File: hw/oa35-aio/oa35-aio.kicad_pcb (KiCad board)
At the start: 6 copper layers, 36 x 36 mm, 283 parts, among them J1 TYPE-C-31-M-12, J10 M1A, J11 M1B, J12 M1C, J13 M2A, J14 M2B, J15 M2C, J16 M3A, J17 M3B, J18 M3C, J19 M4A, J2 SM06B-SRSS-TB, J20 M4B, J21 M4C, J3 BAT+, J4 BAT-, P1 +5V, P10 TX6, P11 RX1, P12 TX1, P13 LED, P14 BZ-, P15 BZ+, P16 RSSI, P17 SCL, P18 SDA, P19 +3V3, P2 GND, P20 GND, P21 VBAT, P22 GND, P3 RX2, P4 TX2, P5 +5V, P6 GND, P7 RX4, P8 TX4, P9 RX6, Q1 2N7002, U1 INA186A3IDCKR, U10 USBLC6-2SC6, U2 LMR51430YFDDCR, U20 AT32F421G8U7, U21 NSG2065Q, U3 LMR51430YFDDCR, U30 AT32F421G8U7, U31 NSG2065Q, U4 LP5912-3.3DRVR, U40 AT32F421G8U7, U41 NSG2065Q, U5 TLV76733DRVR, U50 AT32F421G8U7, U51 NSG2065Q, U6 STM32F722RET6, U7 ICM-42688-P, U8 BMP280, U9 W25Q128JVSIQ, Y1 8MHz

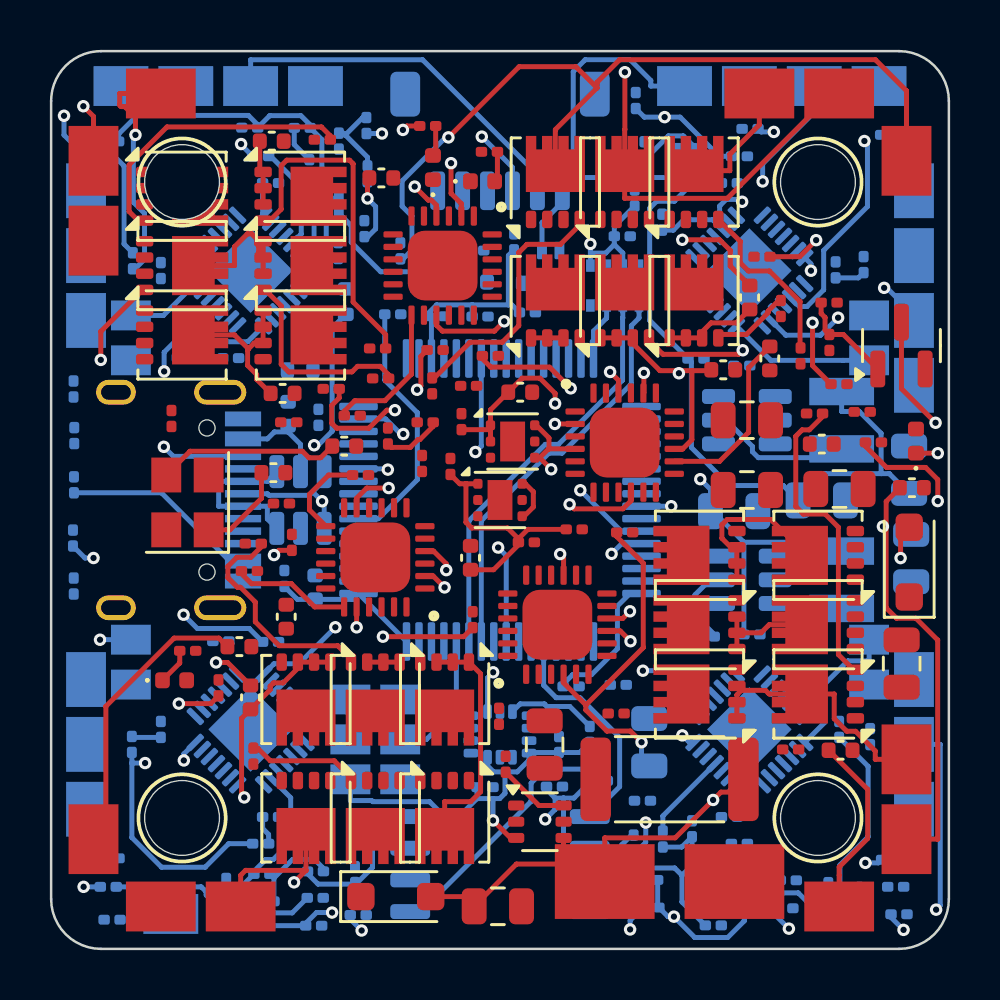
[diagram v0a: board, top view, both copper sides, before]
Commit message: OA35-AIO: regenerate the board at the tighter design rules
Co-Authored-By: Claude Opus 5 <noreply@anthropic.com>
Claude-Session: https://claude.ai/code/session_013J1rgXZWykCJN7jVVS67P2
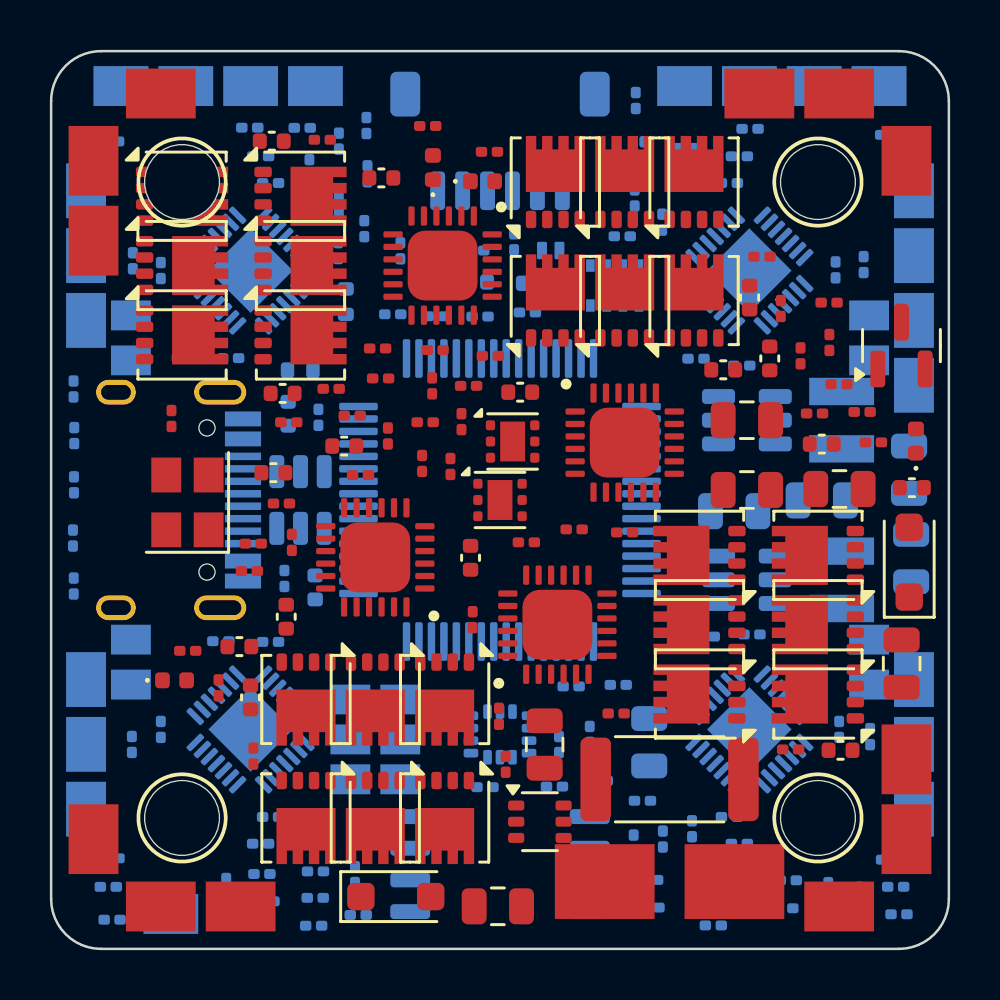
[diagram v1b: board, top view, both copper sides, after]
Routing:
- net +3V3E: track 114.1 -> 0.00 mm, vias 6 -> 0
- net +10V: track 90.3 -> 0.00 mm, vias 8 -> 0
- net +3V3: track 78.3 -> 0.00 mm, vias 4 -> 0
- net PH_B_1: track 49.6 -> 0.00 mm, vias 3 -> 0
- net PH_B_2: track 38.1 -> 0.00 mm, vias 2 -> 0
- net UART1_RX: track 37.3 -> 0.00 mm, vias 3 -> 0
- net PAD_RSSI: track 35.3 -> 0.00 mm, vias 2 -> 0
- net PH_C_2: track 35.3 -> 0.00 mm, vias 1 -> 0
- net PH_B_4: track 34.9 -> 0.00 mm, vias 3 -> 0
- net PAD_BZ-: track 32.3 -> 0.00 mm, vias 2 -> 0
- net VBAT_IN: track 31.7 -> 0.00 mm, vias 2 -> 0
- net ADC_RSSI: track 29.8 -> 0.00 mm, vias 2 -> 0
- net +5V_BUCK: track 28.7 -> 0.00 mm
- net UART4_RX: track 25.9 -> 0.00 mm, vias 2 -> 0
- net FBB_1: track 25.8 -> 0.00 mm, vias 3 -> 0
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
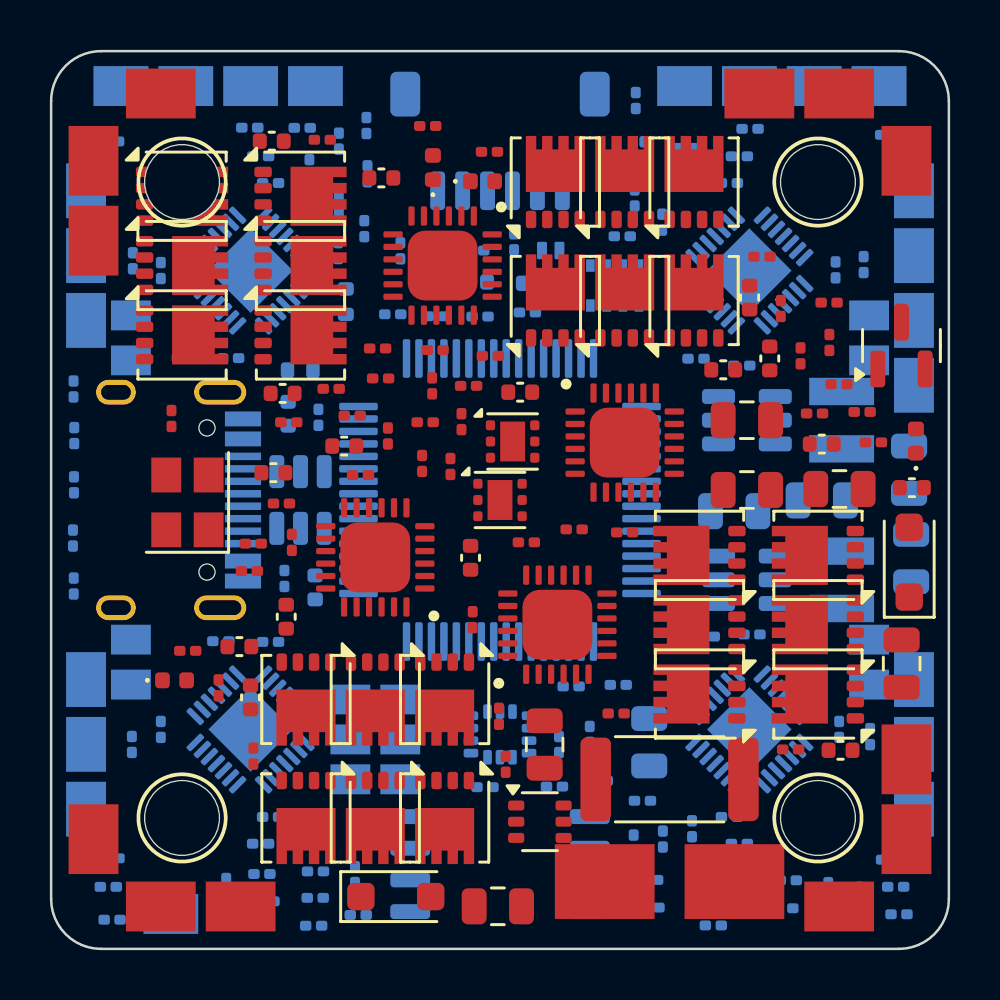
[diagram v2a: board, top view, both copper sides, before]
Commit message: OA35-AIO: rework the floorplan so nothing sits on a mounting hole
The placement checker skipped the mounting holes, and with them out of the
picture all four ESC micros, one MOSFET and a battery pad had drifted on
top of a 3 mm hole.  Holes are now obstacles on both sides, which is what
they are.

Making room for them meant moving the pieces that were boxing each other in:

  - the HD VTX pads are surface mount only, so they take the left edge and
    let channel 4 sit symmetrically with the other three
  - USB-C moves to the front edge, where its through-hole shell posts no
    longer eat into channel 4's power stage on the top side
  - each ESC micro now sits directly under its own channel's MOSFET array,
    keeping the sixty-odd micro-to-driver nets inside one quadrant instead
    of sending them across the middle of the board
  - the bucks, the test pads and four wire pads follow into the space that
    frees up

Also stop tracking __pycache__.

Co-Authored-By: Claude Opus 5 <noreply@anthropic.com>
Claude-Session: https://claude.ai/code/session_013J1rgXZWykCJN7jVVS67P2
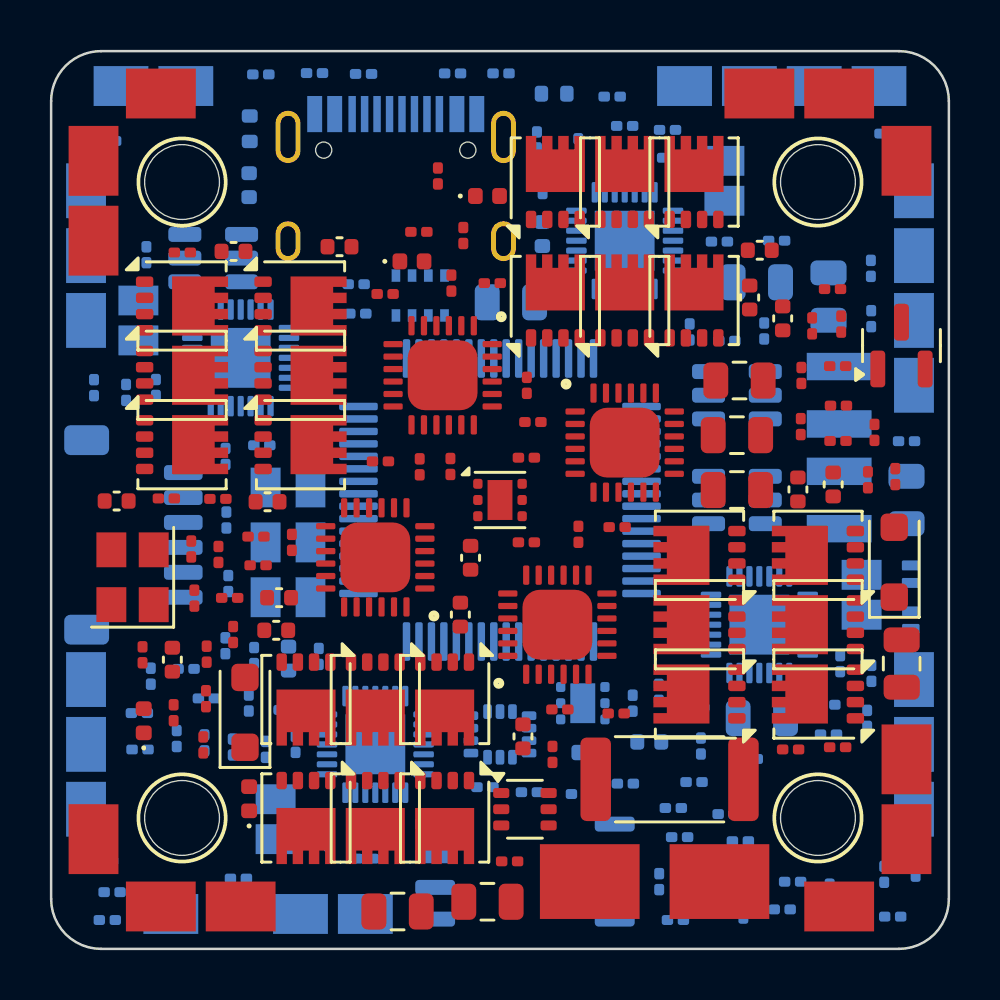
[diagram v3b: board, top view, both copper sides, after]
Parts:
- C23, C24, U5: moved to B.Cu
- R11, R18, RSIG1, RSIG2, RSIG3, RSIG4: moved to F.Cu
- moved RNC2 35.4 mm to (163.2, 115.7)
- moved P3 33.3 mm to (142.0, 116.6)
- moved P4 33.3 mm to (144.6, 116.6)
- moved R15 32.4 mm to (166.7, 114.8), turned to 90 degrees
- moved RNA4 31.6 mm to (157.6, 115.1)
- moved RSIG2 31.3 mm to (148.5, 89.4), turned to 90 degrees
- moved RNC4 31.0 mm to (165.4, 115.0), turned to 90 degrees
- moved D8 30.3 mm to (139.9, 112.0)
- moved RNB4 29.8 mm to (159.8, 116.4)
- moved RCC4 28.9 mm to (134.1, 114.5)
- moved R11 28.7 mm to (138.1, 109.8), turned to 90 degrees
- moved RNB2 28.6 mm to (157.0, 116.8), turned to 0 degrees
- moved RCB4 25.3 mm to (135.6, 110.0)
- moved RBC2 24.9 mm to (156.9, 112.4), turned to 0 degrees
- moved RCC2 24.7 mm to (138.2, 109.7)
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
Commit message: OA35-AIO: give the fine-pitch packages room to fan out, and fix two placer bugs
A 0.4 mm pitch QFN cannot be escaped between its own pads, so every pin has
to leave the package and drop to an inner layer through a via, which needs
about 0.7 mm of ring.  Decoupling packed at 0.3 mm left 0.6 mm, and the
router gave up on those pins; the ten fine-pitch packages now keep an extra
0.75 mm to themselves.

Making room for that exposed two bugs in the placer:

  - falling back to the other board side recursed without remembering it had
    already flipped, so a part that fits on neither side looped until Python
    ran out of stack rather than saying so
  - the footprint's size was measured again for every candidate position,
    which is why a failing placement took ten minutes to fail

And one ordering problem: by neighbour count alone a lone SOT-23 is placed
last, when the free copper is 240 mm2 of 0.6 mm alleys without a single
3.5 x 3 mm hole in it.  Big parts go first now.

route.py can also route in rounds, carrying the previous round's wires into
the next DSN: freerouting only reports once every requested pass is done, so
a twenty-pass run is an hour of silence, while rounds of two cost the same
and can be watched.

Co-Authored-By: Claude Opus 5 <noreply@anthropic.com>
Claude-Session: https://claude.ai/code/session_013J1rgXZWykCJN7jVVS67P2
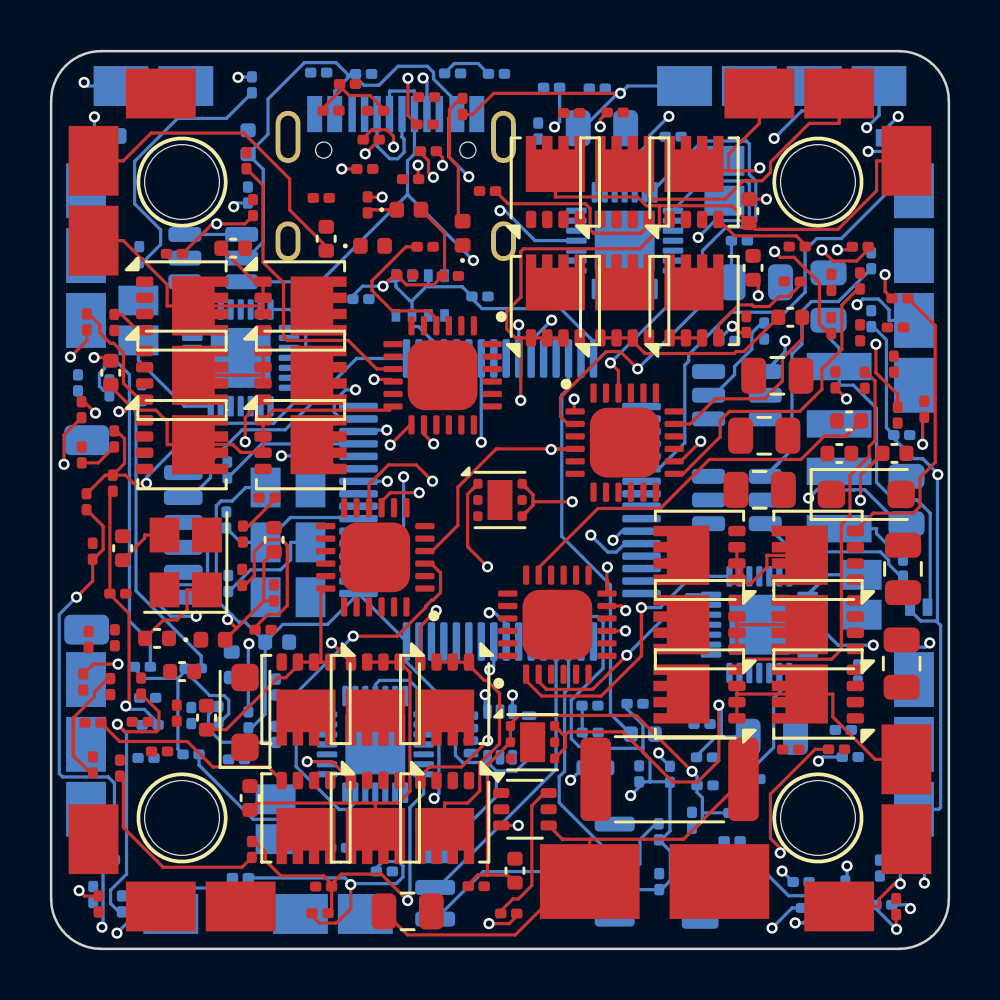
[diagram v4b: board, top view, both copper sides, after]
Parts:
- C23, C24, R14, R15, RCA3, RCA4, RCB2, RCB3, RCB4, RCC2, RCC3, RCC4, RNA1, RNA2, RNA3, RNA4, RNB1, RNB2, RNB4, RNC1, RNC2, RNC3, RNC4, U5: moved to F.Cu
- Q1: moved to B.Cu
- moved RBA2 39.0 mm to (162.1, 115.3)
- moved R15 38.6 mm to (136.9, 90.1), turned to 0 degrees
- moved R14 38.3 mm to (140.1, 88.3), turned to 90 degrees
- moved RBB2 35.5 mm to (163.8, 115.6), turned to 90 degrees
- moved R17 35.3 mm to (133.7, 110.6), turned to 90 degrees
- moved RNC4 34.3 mm to (133.7, 102.1)
- moved R16 32.7 mm to (134.4, 107.5)
- moved RNC3 30.1 mm to (134.8, 110.8)
- moved RNA4 29.7 mm to (133.2, 98.2)
- moved RSIG3 29.5 mm to (144.8, 85.6)
- moved RVDA2 28.6 mm to (157.7, 112.8), turned to 90 degrees
- moved RNB4 28.1 mm to (134.7, 103.8), turned to 0 degrees
- moved RNC1 27.2 mm to (135.6, 107.5), turned to 90 degrees
- moved RNB1 26.9 mm to (135.6, 108.9)
- moved R24 26.3 mm to (139.2, 106.6), turned to 90 degrees
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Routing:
- net +3V3: track 0.00 -> 137.3 mm, vias 0 -> 6
- net +5V: track 0.00 -> 112.0 mm, vias 0 -> 5
- net +10V: track 0.00 -> 76.1 mm, vias 0 -> 4
- net PH_C_2: track 0.00 -> 59.5 mm, vias 0 -> 2
- net FBC_2: track 0.00 -> 51.2 mm, vias 0 -> 3
- net FBC_1: track 0.00 -> 48.0 mm, vias 0 -> 2
- net UART1_RX: track 0.00 -> 43.2 mm, vias 0 -> 3
- net VBUS: track 0.00 -> 41.2 mm, vias 0 -> 2
- net PH_A_2: track 0.00 -> 41.2 mm, vias 0 -> 3
- net PH_C_1: track 0.00 -> 40.5 mm, vias 0 -> 3
- net +3V3E: track 0.00 -> 40.5 mm, vias 0 -> 1
- net CURR: track 0.00 -> 40.4 mm, vias 0 -> 3
- net FBCOM_1: track 0.00 -> 40.1 mm, vias 0 -> 2
- net PH_C_4: track 0.00 -> 38.9 mm, vias 0 -> 2
- net FB_5V: track 0.00 -> 36.5 mm, vias 0 -> 3
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
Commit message: OA35-AIO: show routing progress as nets carrying copper, not as a claim
freerouting prints "Auto-routing was completed" whether or not it managed
to route anything, so route.py now measures the board itself after every
round and draws a bar from it.  GND and VBAT are excluded: they are planes,
they are taken out of the DSN before routing, and counting them would show
the board as permanently short of done.  The router's own output goes to
build/freerouting.log instead of being thrown away.

Co-Authored-By: Claude Opus 5 <noreply@anthropic.com>
Claude-Session: https://claude.ai/code/session_013J1rgXZWykCJN7jVVS67P2
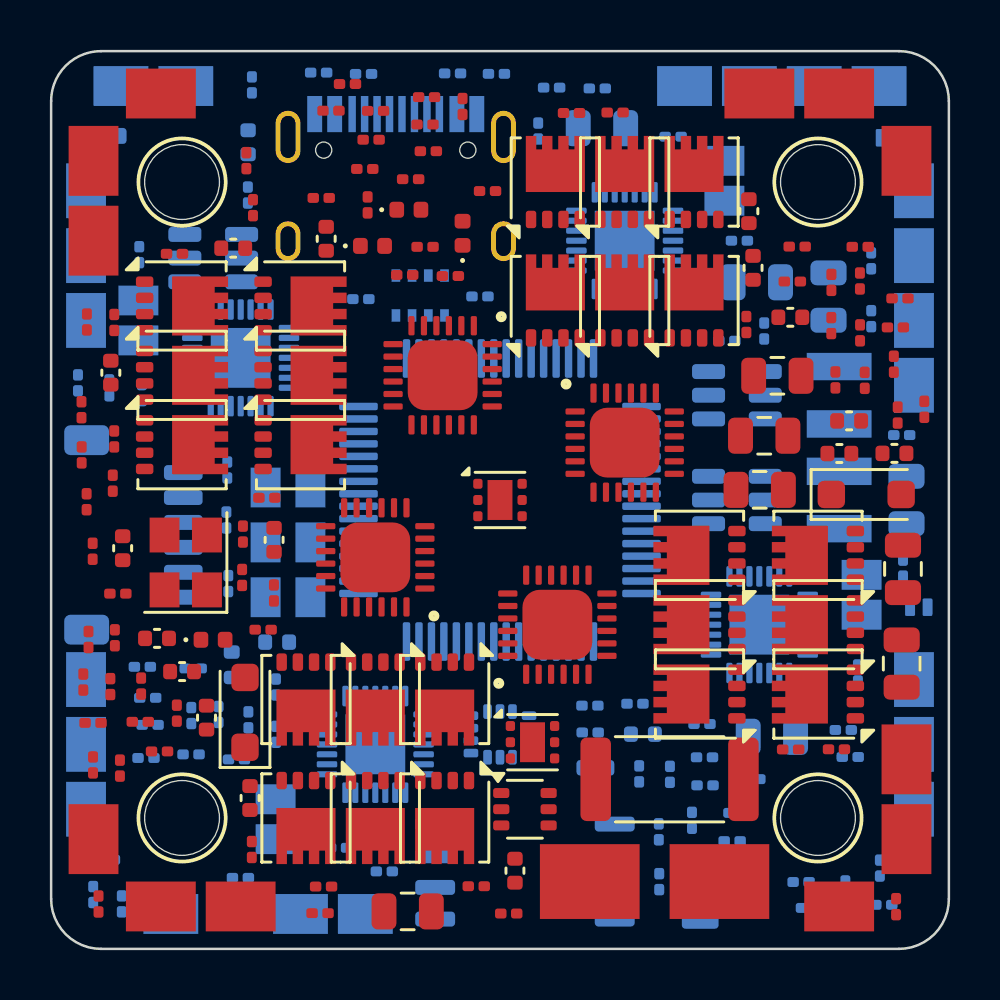
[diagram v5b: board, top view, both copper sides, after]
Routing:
- net +3V3: track 137.3 -> 0.00 mm, vias 6 -> 0
- net +5V: track 112.0 -> 0.00 mm, vias 5 -> 0
- net +10V: track 76.1 -> 0.00 mm, vias 4 -> 0
- net PH_C_2: track 59.5 -> 0.00 mm, vias 2 -> 0
- net FBC_2: track 51.2 -> 0.00 mm, vias 3 -> 0
- net FBC_1: track 48.0 -> 0.00 mm, vias 2 -> 0
- net UART1_RX: track 43.2 -> 0.00 mm, vias 3 -> 0
- net VBUS: track 41.2 -> 0.00 mm, vias 2 -> 0
- net PH_A_2: track 41.2 -> 0.00 mm, vias 3 -> 0
- net PH_C_1: track 40.5 -> 0.00 mm, vias 3 -> 0
- net +3V3E: track 40.5 -> 0.00 mm, vias 1 -> 0
- net CURR: track 40.4 -> 0.00 mm, vias 3 -> 0
- net FBCOM_1: track 40.1 -> 0.00 mm, vias 2 -> 0
- net PH_C_4: track 38.9 -> 0.00 mm, vias 2 -> 0
- net FB_5V: track 36.5 -> 0.00 mm, vias 3 -> 0
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
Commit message: OA35-AIO: routing round 1, 88 of 200 signal nets in copper
Intermediate state; the rounds carry each other's wires forward.

Co-Authored-By: Claude Opus 5 <noreply@anthropic.com>
Claude-Session: https://claude.ai/code/session_013J1rgXZWykCJN7jVVS67P2
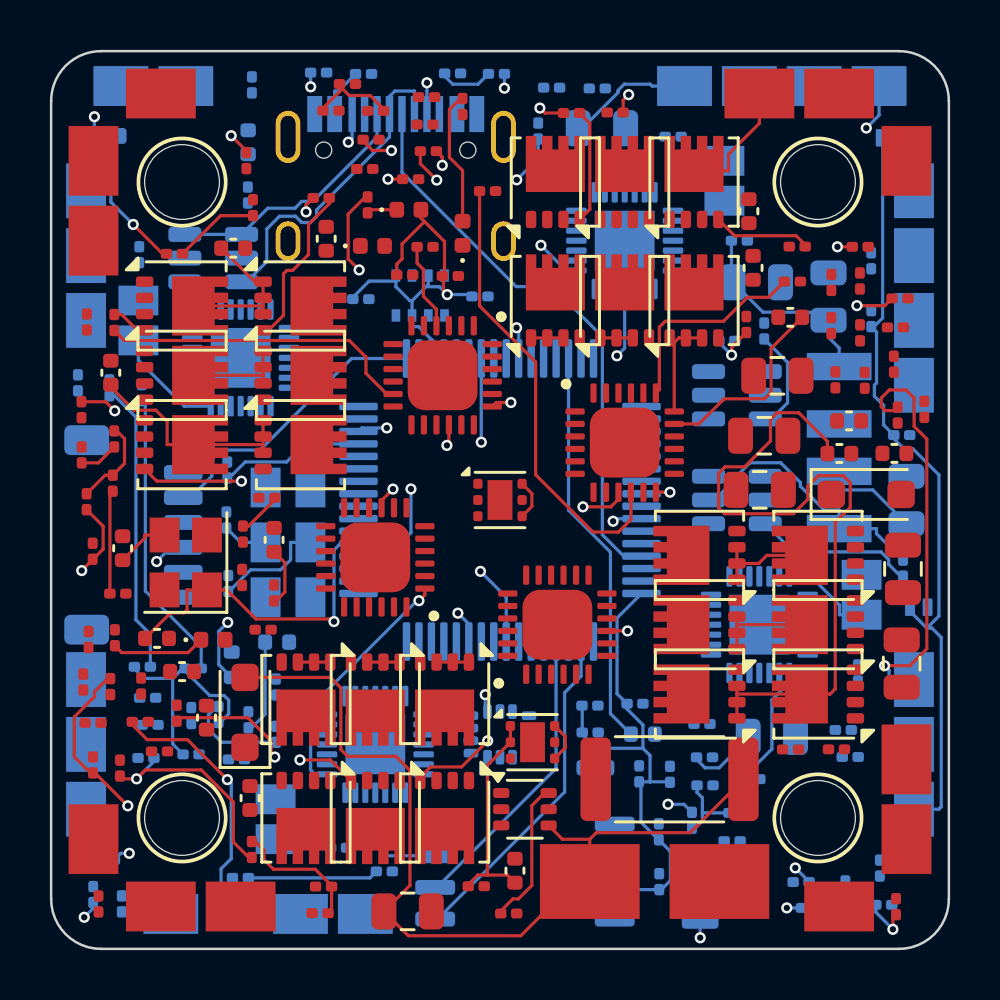
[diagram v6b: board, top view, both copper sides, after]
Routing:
- net +3V3: track 0.00 -> 48.7 mm, vias 0 -> 1
- net FBA_2: track 0.00 -> 40.2 mm, vias 0 -> 3
- net +5V: track 0.00 -> 38.0 mm
- net VBAT_IN: track 0.00 -> 36.2 mm
- net USB_DP: track 0.00 -> 33.2 mm
- net BEEP_G: track 0.00 -> 33.1 mm, vias 0 -> 2
- net VDDA_2: track 0.00 -> 30.6 mm, vias 0 -> 2
- net PH_A_1: track 0.00 -> 28.5 mm
- net GCL_3: track 0.00 -> 27.9 mm, vias 0 -> 2
- net UART4_TX: track 0.00 -> 27.3 mm, vias 0 -> 2
- net CC2: track 0.00 -> 25.0 mm, vias 0 -> 2
- net M3: track 0.00 -> 24.1 mm, vias 0 -> 2
- net I2C_SDA: track 0.00 -> 23.7 mm, vias 0 -> 2
- net UART1_TX: track 0.00 -> 21.5 mm, vias 0 -> 2
- net PH_C_2: track 0.00 -> 21.1 mm, vias 0 -> 2
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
